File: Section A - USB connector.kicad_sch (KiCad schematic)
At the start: 3 parts, among them P1 USB_C_Plug_USB2.0

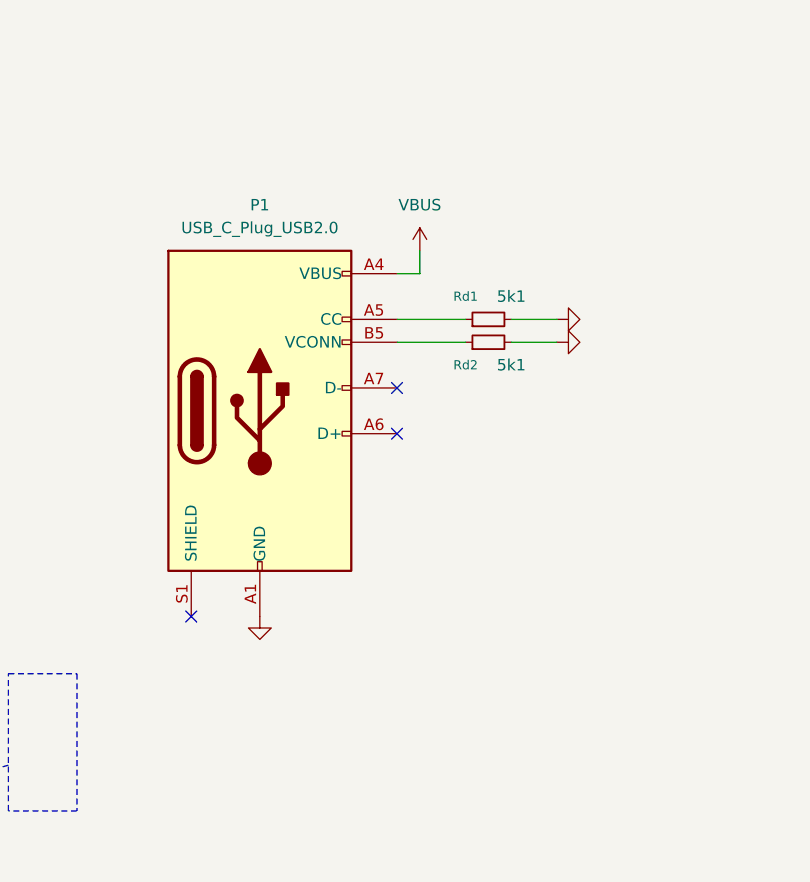
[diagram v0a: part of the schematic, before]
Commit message: schematic file names changed
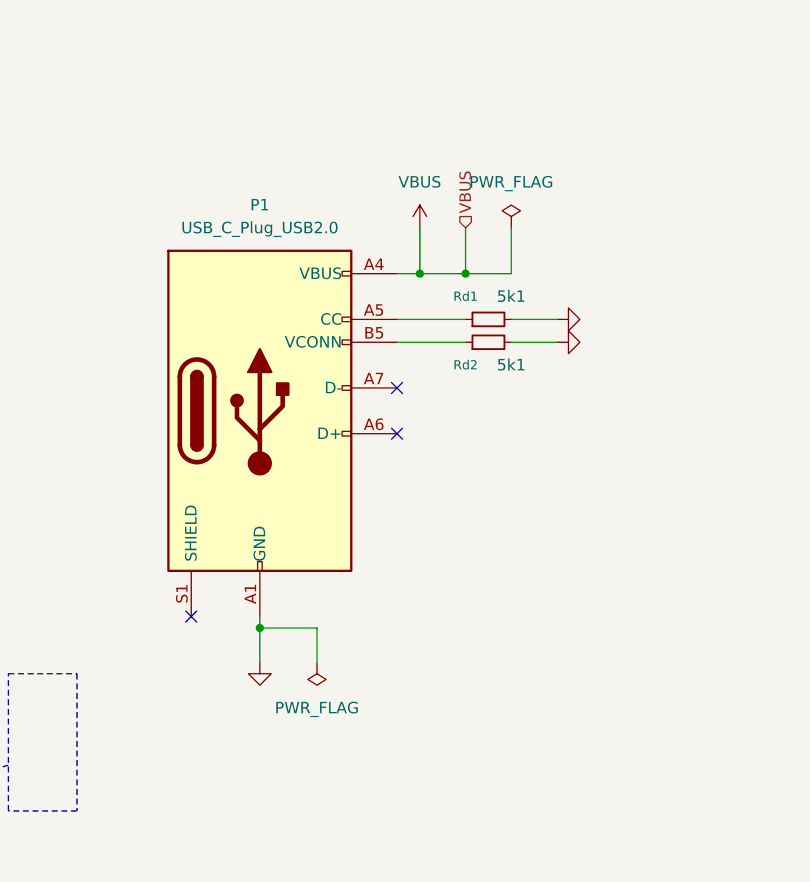
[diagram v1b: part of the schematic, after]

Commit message: board updatea
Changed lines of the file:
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@@
 	(wire
 		(pts
-			(xy 185.42 60.96) (xy 185.42 66.04)
+			(xy 189.23 60.96) (xy 189.23 66.04)
 		)
 		(stroke
@@
 	(wire
 		(pts
-			(xy 180.34 66.04) (xy 185.42 66.04)
+			(xy 180.34 66.04) (xy 189.23 66.04)
 		)
 		(stroke
@@
 	(symbol
 		(lib_id "power:PWR_FLAG")
-		(at 185.42 60.96 0)
+		(at 189.23 60.96 0)
 		(unit 1)
 		(exclude_from_sim no)
@@
 		(fields_autoplaced yes)
 		(property "Reference" "#FLG01"
-			(at 185.42 59.055 0)
+			(at 189.23 59.055 0)
 			(effects
 				(font
@@
 		)
 		(property "Value" "PWR_FLAG"
-			(at 185.42 55.88 0)
+			(at 189.23 55.88 0)
 			(effects
 				(font
@@
 		)
 		(property "Footprint" ""
-			(at 185.42 60.96 0)
+			(at 189.23 60.96 0)
 			(effects
 				(font
@@
 		)
 		(property "Datasheet" "~"
-			(at 185.42 60.96 0)
+			(at 189.23 60.96 0)
 			(effects
 				(font
@@
 		)
 		(property "Description" "Special symbol for telling ERC where power comes from"
-			(at 185.42 60.96 0)
-			(effects
-				(font
+			(at 189.23 60.96 0)
+			(effects
+				(font

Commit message: pcb update
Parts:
- removed P1: USB_C_Plug_USB2.0, __USB4135-GF-A:GCT_USB4135-GF-A_REVA, symbol Connector:USB_C_Plug_USB2.0
- added J?: USB4135-GF-A_REVA, __USB4135-GF-A:GCT_USB4135-GF-A_REVA, symbol __GCT__USB4135-GF-A:USB4135-GF-A_REVA
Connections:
- net GND: now also J?.A12 (GND_A), J?.B12 (GND_B)
- net VBUS: now also J?.A9 (VBUS_A), J?.B9 (VBUS_B)
- net at Rd2.1: now also J?.A5 (CC)
- net at Rd1.1: now also J?.B5 (VCONN)
- new net: J?.S1 (SHIELD), J?.S2 (SHIELD), J?.S3 (SHIELD), J?.S4 (SHIELD)
- no-connect marks 3 -> 1
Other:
- moved on the sheet: Rd1, Rd2

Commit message: pcb update
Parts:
- gave numbers to parts that had none: 1
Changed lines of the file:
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@@
 		(dnp no)
 		(fields_autoplaced yes)
-		(property "Reference" "J?"
+		(property "Reference" "J2"
 			(at 125.73 69.8499 0)
 			(effects
@@
 			(project ""
 				(path "/f9e05184-c88b-4a88-ae9c-ab2bdb32be7c/c5103ceb-5325-4a84-a025-9638a412984e/f06537ee-772d-44d3-8c50-e0ba41038c9c"
-					(reference "J?")
+					(reference "J2")
 					(unit 1)
 				)

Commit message: touch pad library creation
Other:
- note added: "www.usb.org/sites/default/files/USB%20Type-C%20Spec%20R2.0%20-%20August%202019.pdf"
- moved on the sheet: J2, Rd1, Rd2

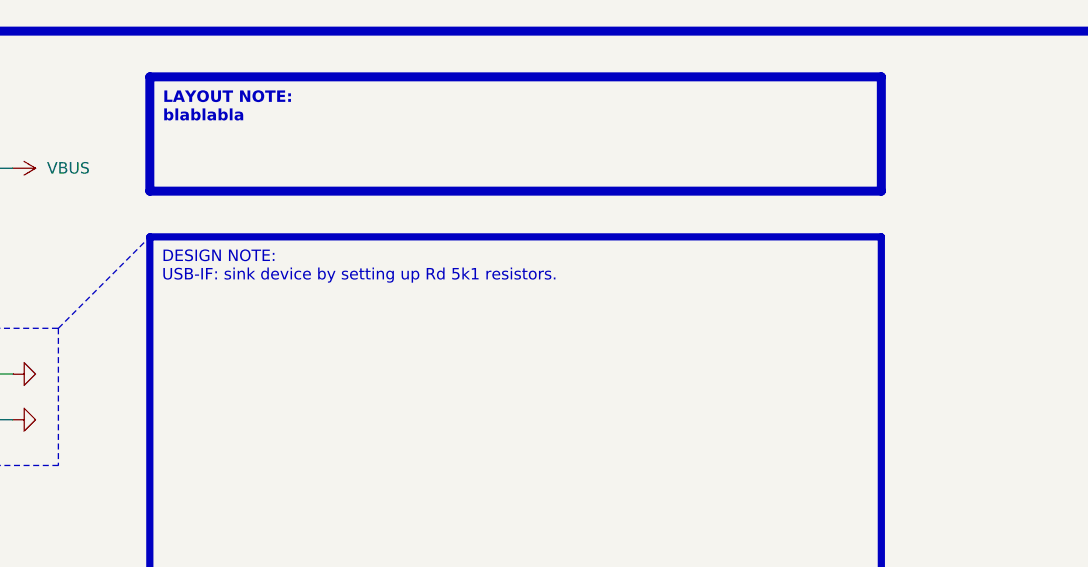
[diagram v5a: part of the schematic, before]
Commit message: minor updates of shematic and pcb and touch pad library
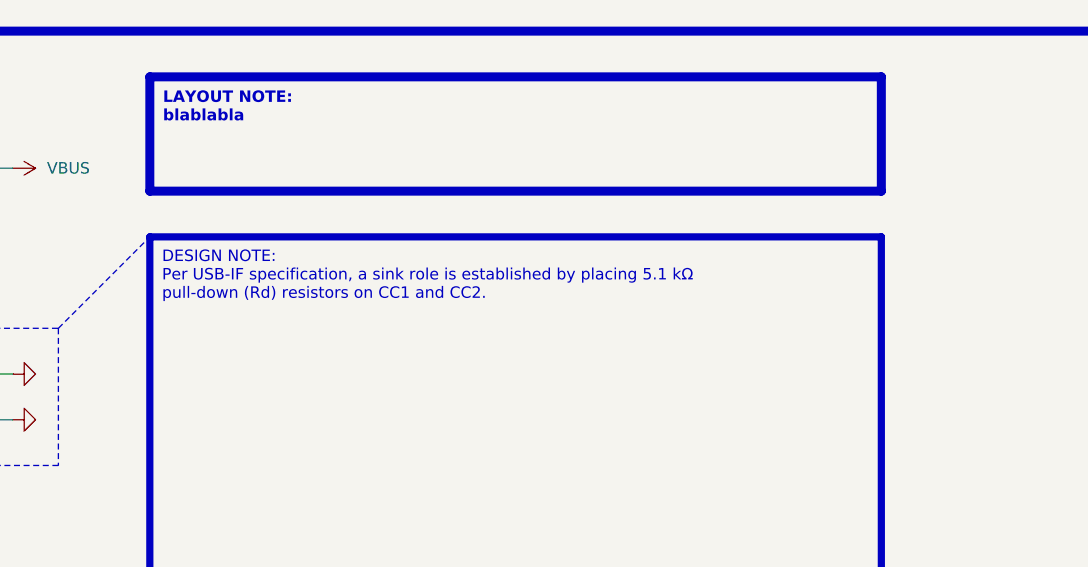
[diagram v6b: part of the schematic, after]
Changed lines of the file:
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@@
 		)
 	)
-	(text_box "DESIGN NOTE:\nUSB-IF: sink device by setting up Rd 5k1 resistors."
+	(text_box "DESIGN NOTE:\nPer USB-IF specification, a sink role is established by placing 5.1 kΩ pull-down (Rd) resistors on CC1 and CC2."
 		(exclude_from_sim no)
 		(at 149.86 58.42 0)

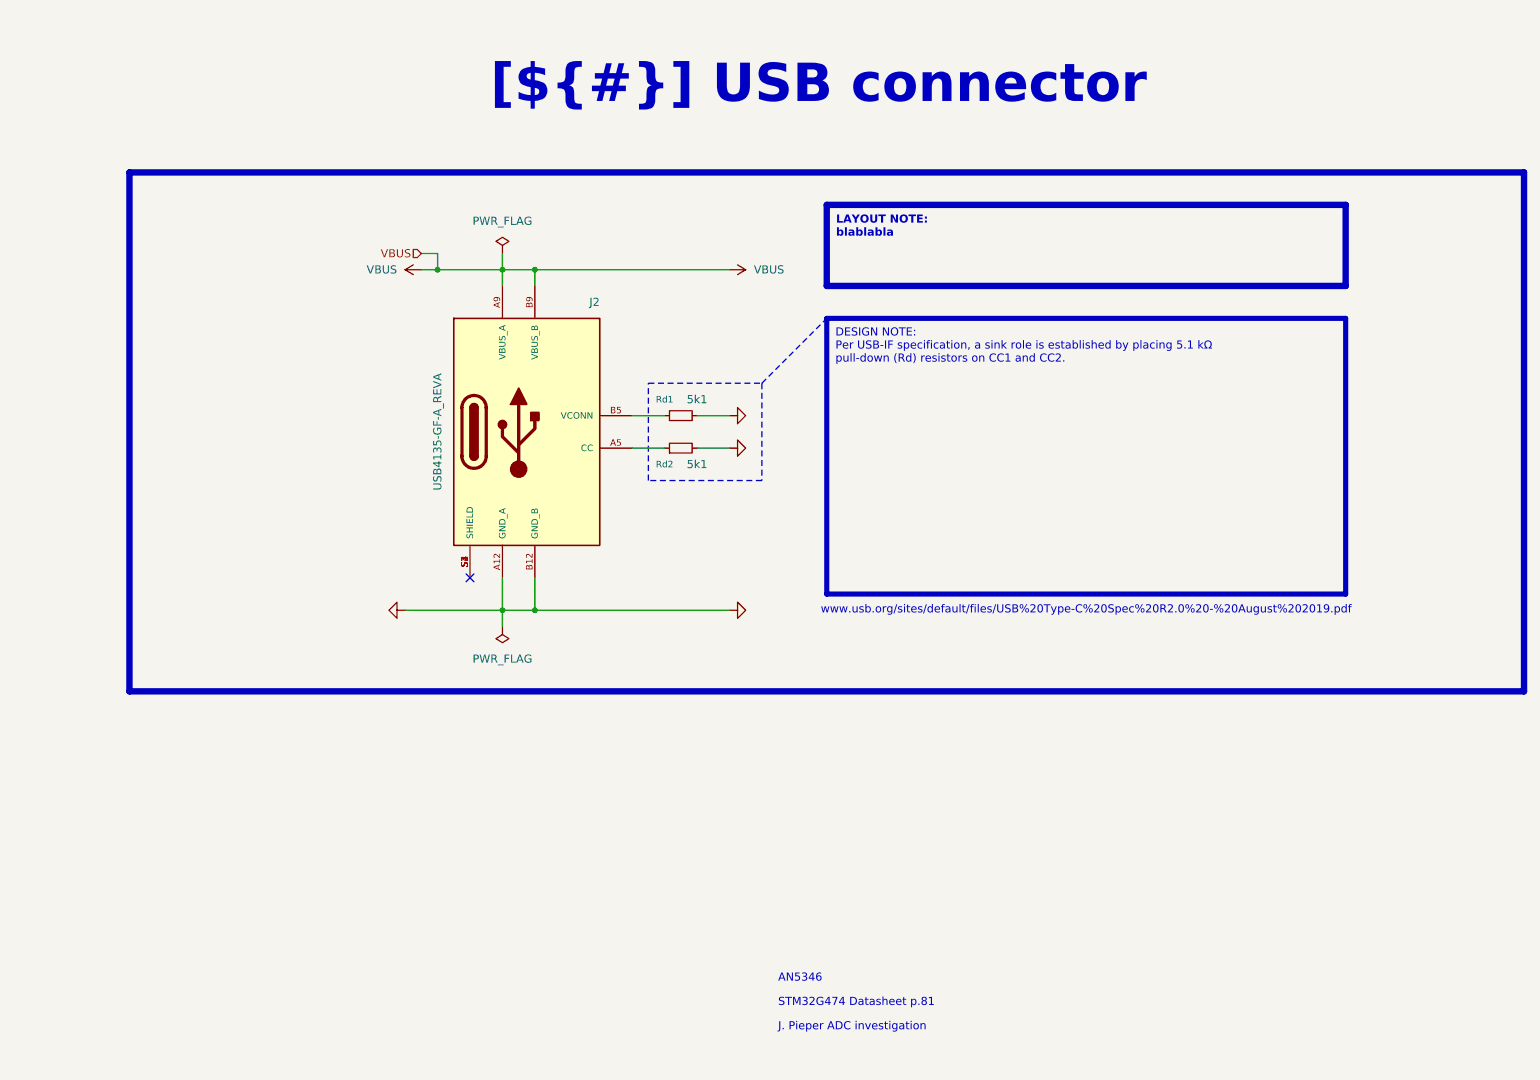
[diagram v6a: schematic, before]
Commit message: [sch] update touch sensor section
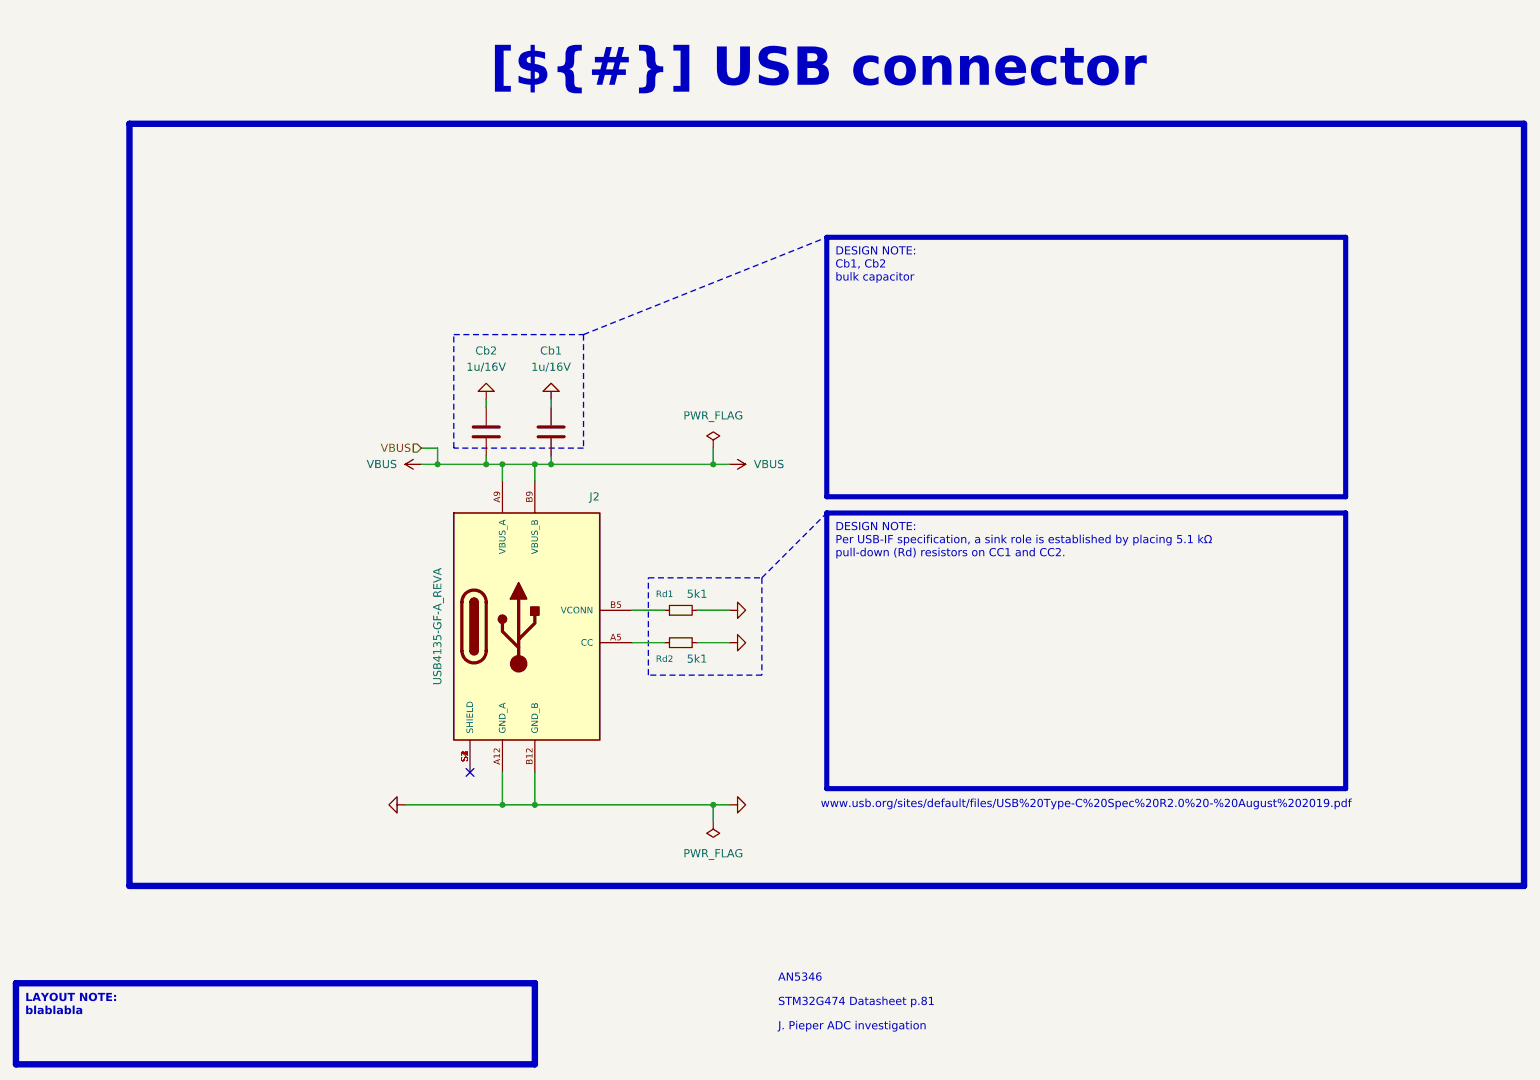
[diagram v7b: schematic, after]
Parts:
- added Cb1, Cb2: 1u/16V, Capacitor_SMD:C_0805_2012Metric, symbol Device:C
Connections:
- net GND: now also Cb1.1, Cb2.1
- net VBUS: now also Cb1.2, Cb2.2
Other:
- moved on the sheet: J2, Rd1, Rd2
